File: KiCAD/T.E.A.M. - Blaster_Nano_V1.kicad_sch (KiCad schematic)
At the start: 26 parts, among them J1 USB_C_Receptacle_USB2.0_14P, J2 Conn_01x02, J3 Conn_01x02, J4 Conn_01x02, J5 Conn_01x02, Q1 FS8205A, U1 TP4056-42-ESOP8, U2 DW01A, U3 MT3608

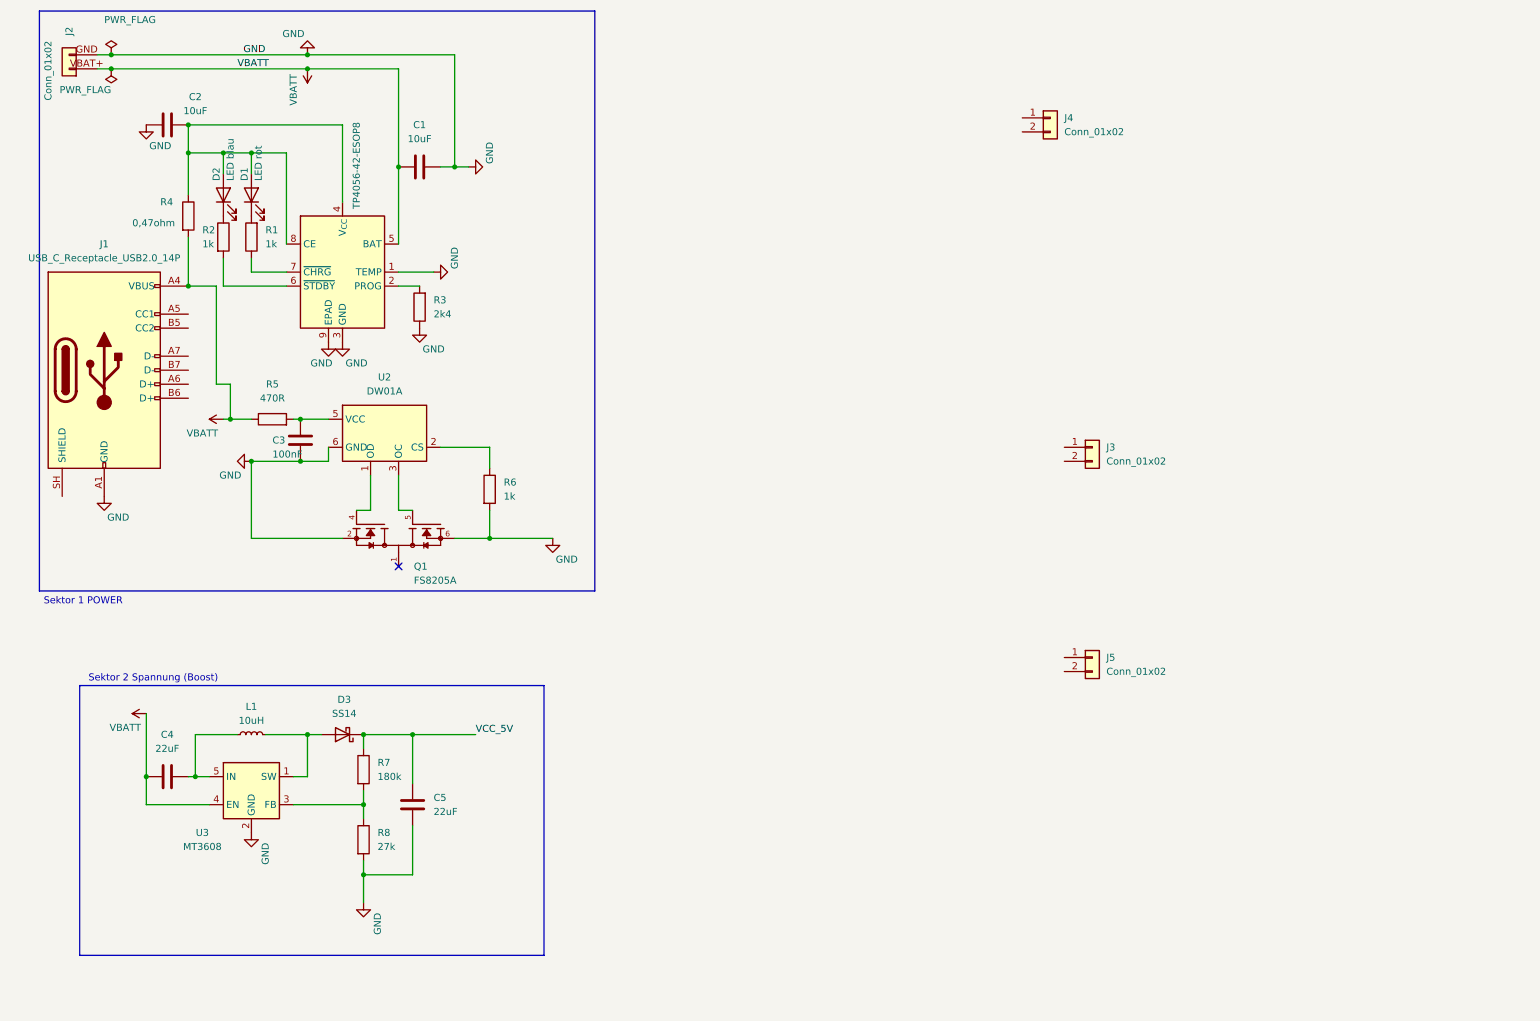
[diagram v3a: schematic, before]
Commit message: Sektor 3 MIKROCONTROLLER - ATmega328P-Au und 6 Pinheader verdrahtet.
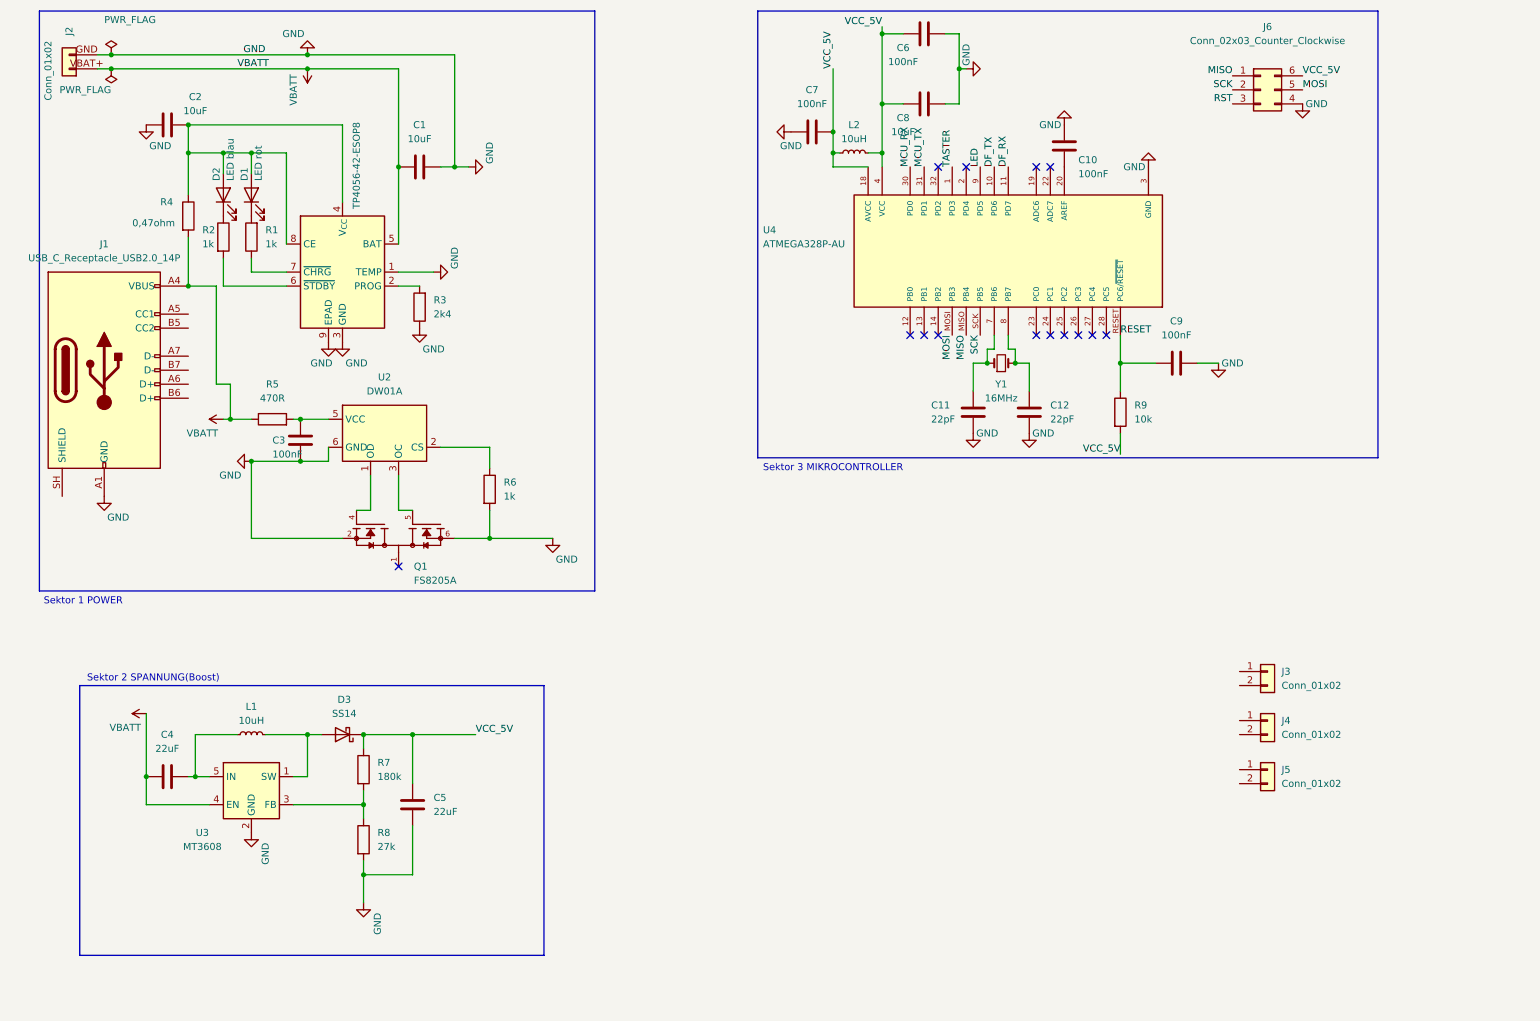
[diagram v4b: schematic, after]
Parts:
- added C10, C6, C7, C9: 100nF, symbol Device:C
- added C11, C12: 22pF, symbol Device:C
- added C8: 10uF, symbol Device:C
- added J6: Conn_02x03_Counter_Clockwise, symbol Connector_Generic:Conn_02x03_Counter_Clockwise
- added L2: 10uH, symbol Device:L_Small
- added R9: 10k, symbol Device:R
- added U4: ATMEGA328P-AU, ATMEGA328P-AU:QFP80P900X900X120-32N, symbol ATMEGA328P-AU:ATMEGA328P-AU
- added Y1: 16MHz, SparkFun-Clock:Crystal-SMD-5x3.2mm, symbol SparkFun-Clock:Crystal
- J2: Funktion (none) -> Anschluss Akku
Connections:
- net GND: now also C10.1, C11.2, C12.2, C6.2, C7.1, C8.2, C9.2, J6.4 (Pin_4), U4.21 (GND), U4.3 (GND), U4.5 (GND)
- net VCC_5V renamed VCC
- net VCC: now also C6.1, C7.2, C8.1, J6.6 (Pin_6), L2.1, L2.2, R9.2, U4.18 (AVCC), U4.4 (VCC), U4.6 (VCC)
- new net: C11.1, U4.7 (PB6), Y1.1
- new net: C12.1, U4.8 (PB7), Y1.2
- new net: C10.2, U4.20 (AREF)
- new net DF_RX: U4.11 (PD7)
- new net DF_TX: U4.10 (PD6)
- new net LED: U4.9 (PD5)
- new net MCU_RX: U4.30 (PD0)
- new net MCU_TX: U4.31 (PD1)
- new net MISO: J6.1 (Pin_1), U4.MISO (PB4)
- new net MOSI: J6.5 (Pin_5), U4.MOSI (PB3)
- new net RESET: C9.1, R9.1, U4.RESET (PC6/~{RESET})
- new net RST: J6.3 (Pin_3)
- new net SCK: J6.2 (Pin_2), U4.SCK (PB5)
- new net TASTER: U4.1 (PD3)
- no-connect marks 1 -> 14
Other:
- note added: "Sektor 2 SPANNUNG(Boost)"
- note added: "Sektor 3 MIKROCONTROLLER"
- note removed: "Sektor 2 Spannung (Boost)"
- moved on the sheet: J3, J4, J5

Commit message: Sektor 4 USB/PROGRAMMER - CH340G verdrahtet.
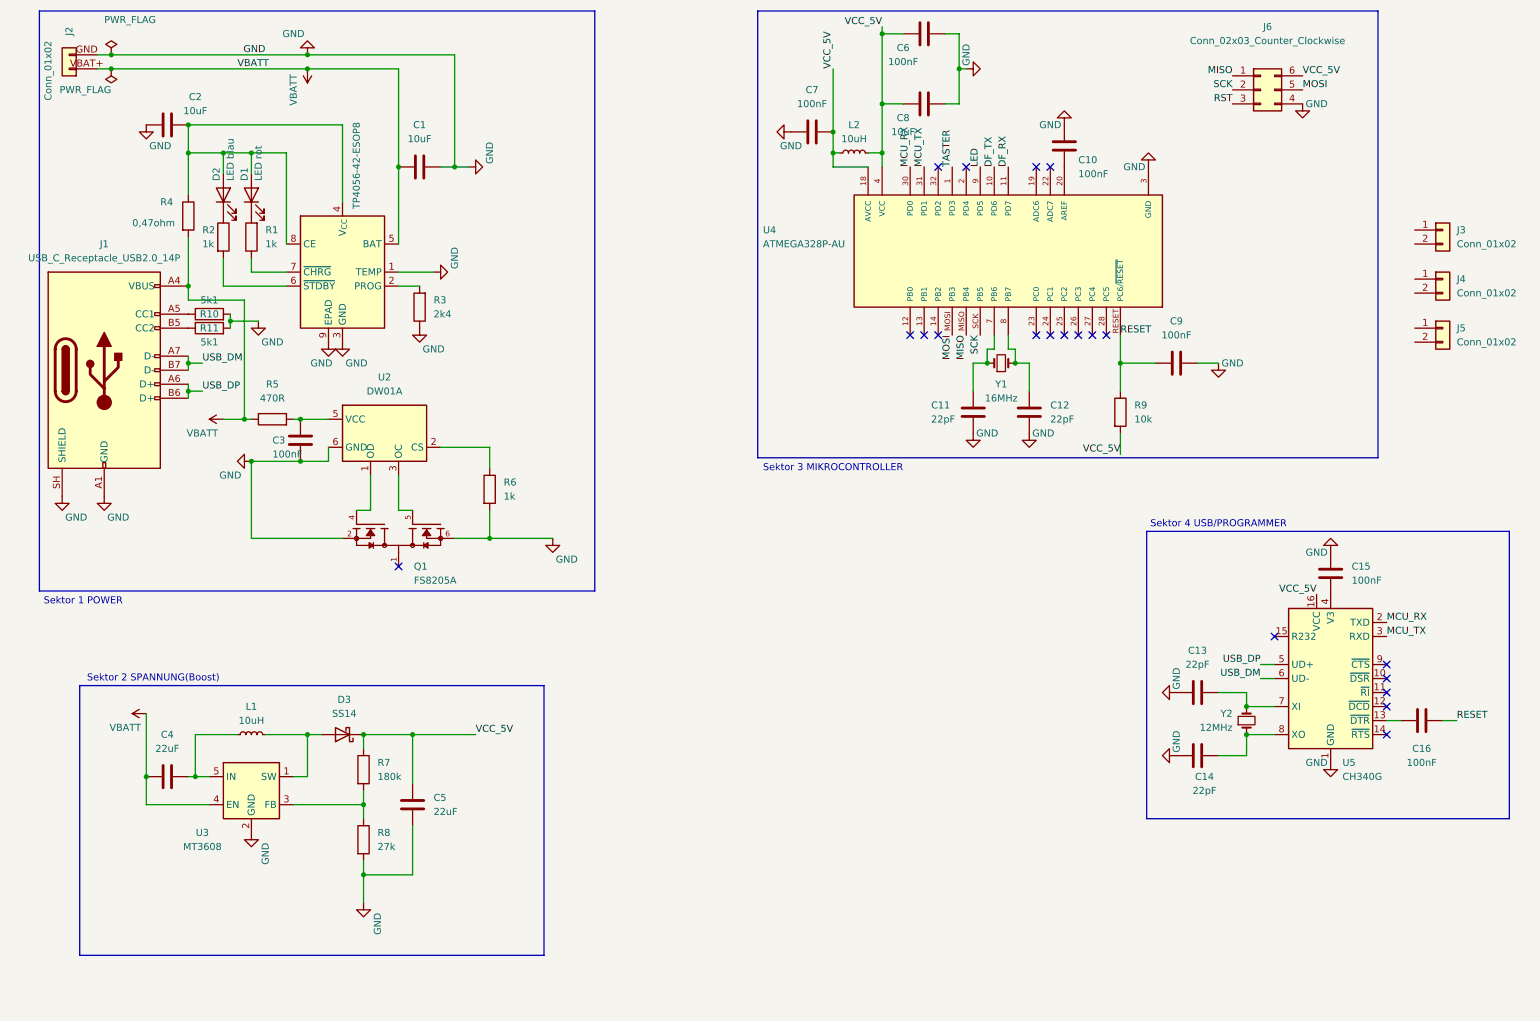
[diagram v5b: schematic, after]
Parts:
- added C13, C14: 22pF, symbol Device:C
- added C15, C16: 100nF, symbol Device:C
- added R10, R11: 5k1, symbol Device:R
- added U5: CH340G, Package_SO:SOIC-16_3.9x9.9mm_P1.27mm, symbol Interface_USB:CH340G
- added Y2: 12MHz, SparkFun-Clock:Crystal-SMD-5x3.2mm, symbol SparkFun-Clock:Crystal
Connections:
- net GND: now also J1.SH (SHIELD), C13.1, C14.1, C15.1, R10.2, R11.2, U5.1 (GND)
- net MCU_RX: now also U5.2 (TXD)
- net MCU_TX: now also U5.3 (RXD)
- net RESET: now also C16.2
- net VCC: now also U5.16 (VCC)
- net at J1.A5 (CC1): now also R10.1
- net USB_DP: now reaches J1.A6 (D+)
- net USB_DP: now also J1.B6 (D+), U5.5 (UD+)
- net USB_DM: now reaches J1.A7 (D-)
- net USB_DM: now also J1.B7 (D-), U5.6 (UD-)
- net at J1.B5 (CC2): now also R11.1
- new net: C13.2, U5.7 (XI), Y2.2
- new net: C14.2, U5.8 (XO), Y2.1
- new net: C16.1, U5.13 (~{DTR})
- new net: C15.2, U5.4 (V3)
- no-connect marks 14 -> 20
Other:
- note added: "Sektor 4 USB/PROGRAMMER"
- moved on the sheet: J3, J4, J5

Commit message: Sektor 5 SOUND UND JST-XH 2,5MM 2-PIN verdrahtet.
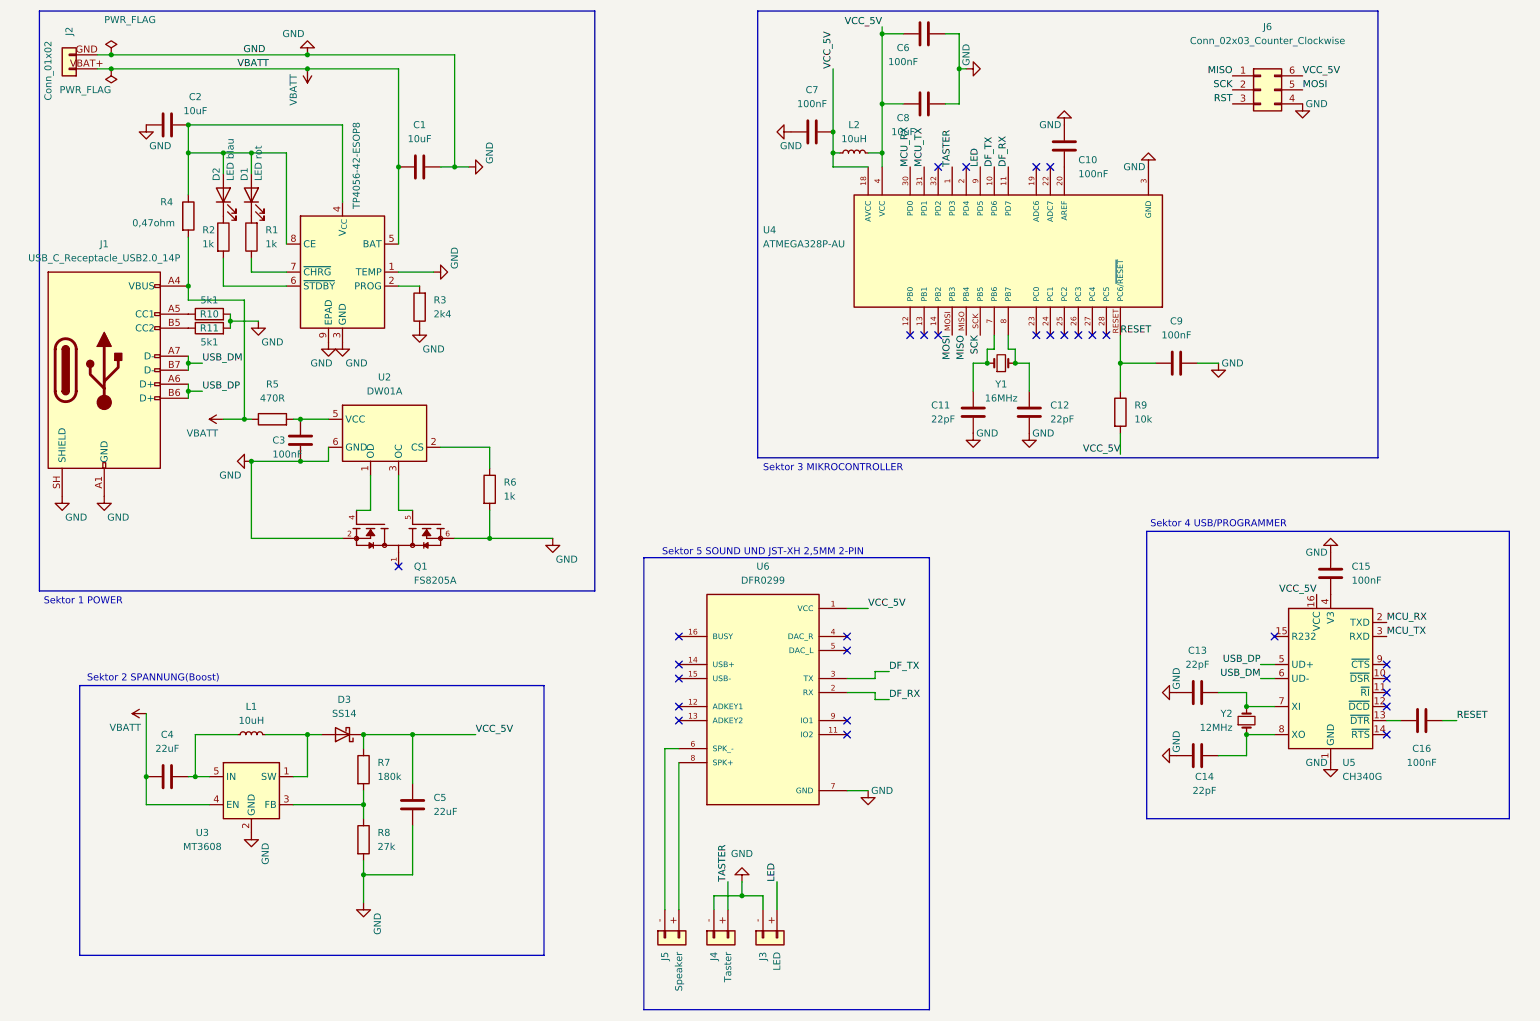
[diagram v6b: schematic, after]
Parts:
- added U6: DFR0299, DFR0299:MODULE_DFR0299, symbol TEAM_Custom:DFR0299
- J3: value Conn_01x02 -> LED; Funktion (none) -> LED
- J4: value Conn_01x02 -> Taster; Funktion (none) -> Taster
- J5: value Conn_01x02 -> Speaker; Funktion (none) -> Speaker
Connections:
- net DF_RX: now also U6.2 (RX)
- net DF_TX: now also U6.3 (TX)
- net GND: now also J3.- (Pin_1), J4.- (Pin_1), U6.10 (GND), U6.7 (GND)
- net LED: now also J3.+ (Pin_2)
- net TASTER: now also J4.+ (Pin_2)
- net VCC: now also U6.1 (VCC)
- new net: J5.+ (Pin_2), U6.8 (SPK+)
- new net: J5.- (Pin_1), U6.6 (SPK_-)
- no-connect marks 20 -> 29
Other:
- note added: "Sektor 5 SOUND UND JST-XH 2,5MM 2-PIN"
- moved on the sheet: J3, J4, J5

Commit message: ERC bereinigt - 0 Fehler, 4 Footprints Warnungen.
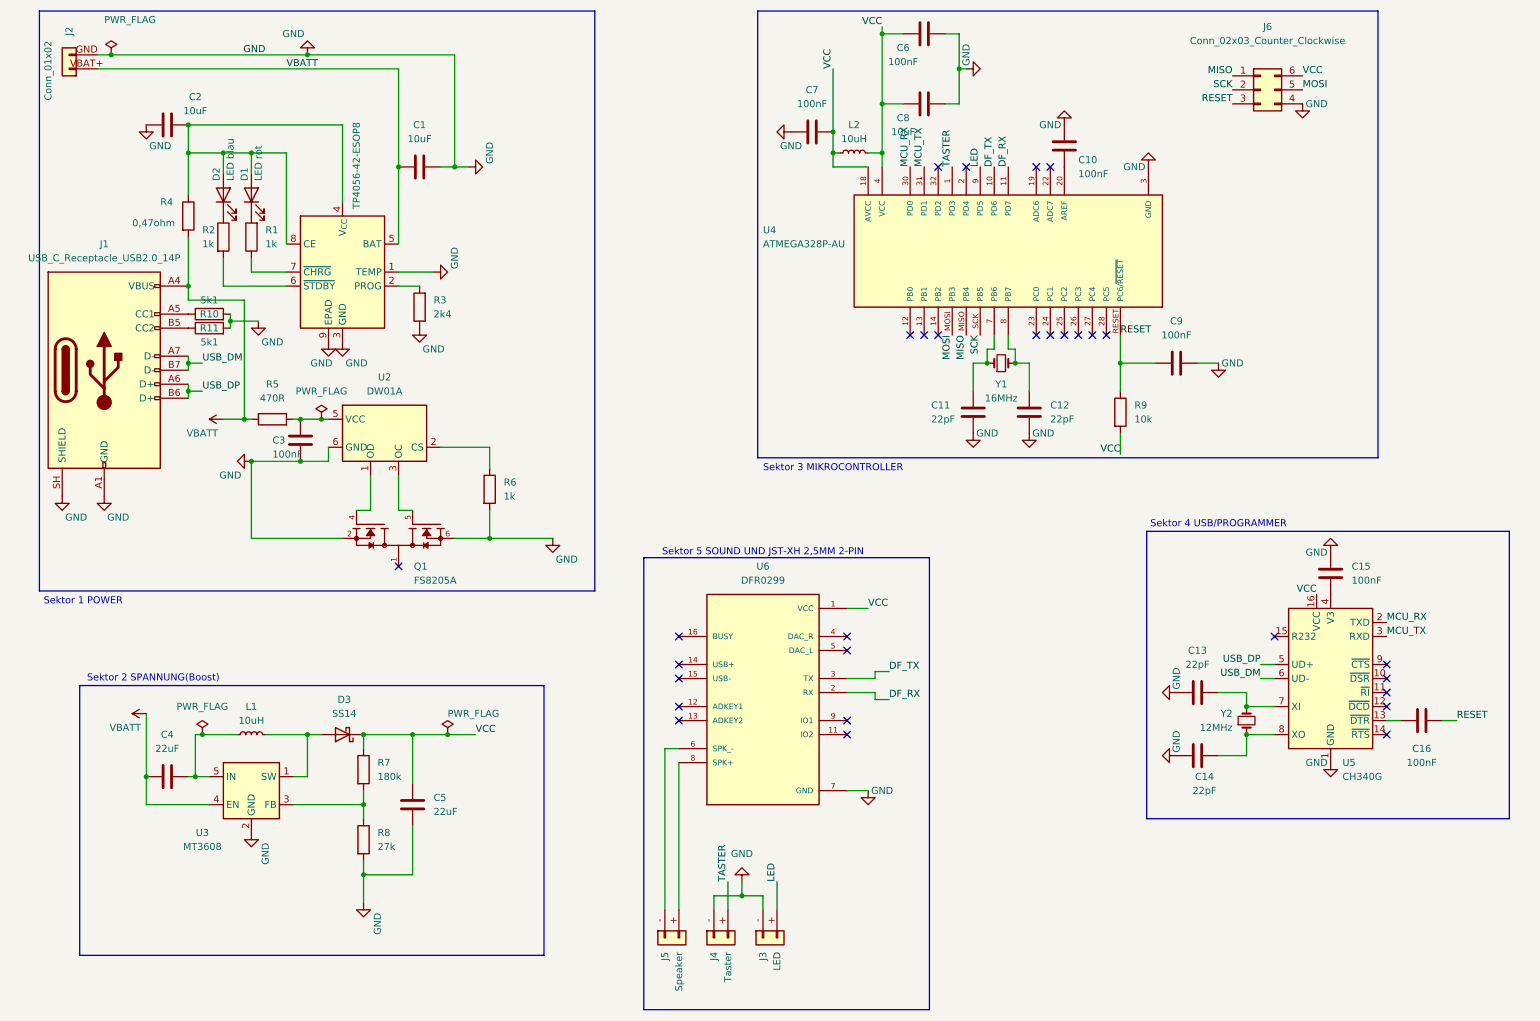
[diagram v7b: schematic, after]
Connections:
- net RST is gone; now on net RESET: J6.3 (Pin_3)
